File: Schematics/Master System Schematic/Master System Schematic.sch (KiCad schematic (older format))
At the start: 34 parts, among them J1 GND, J2 TS+, J3 TS-, SW1 GLVMS, SW2 SideMounted (BRB), SW3 SideMounted (BRB), U1 CAN_Module

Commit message: Fixed a weird duplicate onto master
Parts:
- removed A1: Arduino_UNO_rev3, symbol NER:Arduino_UNO_rev3
- removed R? (x2): R, symbol Device:R
- removed U1: CAN_Module, symbol NER:CAN-Module
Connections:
- net labels removed: CAN_H, CAN_L, GLV+, GLV_GND, POT1+, POT1-, POT1_INPUT, POT2+, POT2-, POT2_INPUT, Switch1-, Switch2-, Switch_Input1, Switch_Input2
- wire segments 225 -> 165
- no-connect marks 26 -> 0
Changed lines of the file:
@@
 EESchema Schematic File Version 4
+LIBS:Master System Schematic-cache
 EELAYER 30 0
 EELAYER END
@@
 Connection ~ 6150 2350
 Wire Wire Line
-	6150 4800 6150 5100
-Wire Wire Line
 	6150 4400 6150 3550
 Wire Notes Line
@@
 	1    0    0    -1
 $EndComp
-Text HLabel 6600 3050 2    50   Input ~ 0
-GLV+
-Wire Wire Line
-	6600 3050 5550 3050
-Text HLabel 3600 3050 0    50   Input ~ 0
-GLV_GND
-Wire Wire Line
-	3600 3050 4350 3050
-$Comp
-L NER:Arduino_UNO_rev3 A1
-U 1 1 5F6833F8
-P 4950 2900
-F 0 "A1" H 4950 3015 50  0000 C CNN
-F 1 "Arduino_UNO_rev3" H 4950 2924 50  0000 C CNN
-F 2 "" H 4950 3050 50  0001 C CNN
-F 3 "" H 4950 3050 50  0001 C CNN
-	1    4950 2900
-	1    0    0    -1
-$EndComp
-$Comp
-L NER:CAN-Module U1
-U 1 1 5F6A22C3
-P 7600 3100
-F 0 "U1" H 7625 3115 50  0000 C CNN
-F 1 "CAN_Module" H 7625 3024 50  0000 C CNN
-F 2 "" H 7600 3100 50  0001 C CNN
-F 3 "" H 7600 3100 50  0001 C CNN
-	1    7600 3100
-	1    0    0    -1
-$EndComp
-Wire Wire Line
-	7050 3450 5900 3450
-Wire Wire Line
-	5900 3450 5900 3650
-Wire Wire Line
-	5900 3650 5550 3650
-Wire Wire Line
-	7050 3550 6100 3550
-Wire Wire Line
-	6100 3550 6100 3850
-Wire Wire Line
-	6100 3850 5550 3850
-Wire Wire Line
-	7050 3650 6250 3650
-Wire Wire Line
-	6250 3650 6250 3750
-Wire Wire Line
-	6250 3750 5550 3750
-Wire Wire Line
-	7050 3750 6350 3750
-Wire Wire Line
-	6350 3750 6350 3950
-Wire Wire Line
-	7050 3850 6600 3850
-Wire Wire Line
-	6600 3850 6600 3400
-Wire Wire Line
-	6600 3400 5750 3400
-Wire Wire Line
-	5750 3400 5750 3550
-Wire Wire Line
-	5750 3550 5550 3550
-Text HLabel 8950 3650 2    50   Input ~ 0
-CAN_L
-Text HLabel 8950 3500 2    50   Input ~ 0
-CAN_H
-Wire Wire Line
-	8200 3500 8600 3500
-Wire Wire Line
-	8950 3650 8200 3650
-NoConn ~ 4350 3200
-NoConn ~ 4350 3300
-NoConn ~ 4350 3400
-NoConn ~ 4350 3500
-Wire Wire Line
-	5550 4700 5900 4700
-Wire Wire Line
-	5900 4700 5900 4900
-Connection ~ 5900 4700
-$Comp
-L Device:R R?
-U 1 1 5F71A5F5
-P 5900 5050
-F 0 "R?" H 5970 5096 50  0000 L CNN
-F 1 "R" H 5970 5005 50  0000 L CNN
-F 2 "" V 5830 5050 50  0001 C CNN
-F 3 "~" H 5900 5050 50  0001 C CNN
-	1    5900 5050
-	1    0    0    -1
-$EndComp
-$Comp
-L Device:R R?
-U 1 1 5F71A986
-P 6150 5050
-F 0 "R?" H 6220 5096 50  0000 L CNN
-F 1 "R" H 6220 5005 50  0000 L CNN
-F 2 "" V 6080 5050 50  0001 C CNN
-F 3 "~" H 6150 5050 50  0001 C CNN
-	1    6150 5050
-	1    0    0    -1
-$EndComp
-Wire Wire Line
-	5900 5200 5900 5400
-Wire Wire Line
-	5900 5400 6000 5400
-NoConn ~ 7050 3350
-NoConn ~ 5550 3250
-NoConn ~ 5550 3350
-NoConn ~ 5550 3450
-NoConn ~ 4350 3650
-NoConn ~ 4350 3750
-NoConn ~ 4350 3850
-NoConn ~ 4350 3950
-NoConn ~ 4350 4350
-NoConn ~ 4350 4700
-NoConn ~ 4350 4800
-NoConn ~ 4350 4900
-NoConn ~ 4350 5000
-NoConn ~ 5550 5000
-NoConn ~ 5550 4900
-NoConn ~ 5550 4600
-NoConn ~ 5550 4500
-NoConn ~ 5550 4400
-NoConn ~ 5550 4300
-NoConn ~ 5550 4150
-NoConn ~ 5550 4050
-Text HLabel 6800 4700 2    50   Input ~ 0
-Switch_Input1
-Text HLabel 6800 5050 2    50   Input ~ 0
-Switch_Input2
-Wire Wire Line
-	4350 4250 3950 4250
-Wire Wire Line
-	3950 4250 3950 4600
-Wire Wire Line
-	3950 5650 6000 5650
-Wire Wire Line
-	6600 5650 6600 5150
-Wire Wire Line
-	6600 4600 6800 4600
-Wire Wire Line
-	5900 4700 6800 4700
-Wire Wire Line
-	6150 4900 6150 4800
-Wire Wire Line
-	5550 4800 6150 4800
-Wire Wire Line
-	6150 4800 6400 4800
-Wire Wire Line
-	6400 4800 6400 5050
-Wire Wire Line
-	6400 5050 6800 5050
-Connection ~ 6150 4800
-Wire Wire Line
-	6600 5150 6800 5150
-Connection ~ 6600 5150
-Wire Wire Line
-	6600 5150 6600 4600
-Text HLabel 6800 5150 2    50   Input ~ 0
-Switch2-
-Text HLabel 6800 4600 2    50   Input ~ 0
-Switch1-
-Wire Wire Line
-	4350 4500 3300 4500
-Wire Wire Line
-	3950 4600 3300 4600
-Connection ~ 3950 4600
-Wire Wire Line
-	3950 4600 3950 5100
-Wire Wire Line
-	4350 4600 4150 4600
-Wire Wire Line
-	4150 4600 4150 5000
-Wire Wire Line
-	4350 4050 3850 4050
-Wire Wire Line
-	3850 4050 3850 4400
-Wire Wire Line
-	3850 4400 3300 4400
-Wire Wire Line
-	3850 4400 3850 4900
-Wire Wire Line
-	3850 4900 3300 4900
-Connection ~ 3850 4400
-Wire Wire Line
-	3950 5100 3300 5100
-Connection ~ 3950 5100
-Wire Wire Line
-	3950 5100 3950 5650
-Text HLabel 3300 4400 0    50   Input ~ 0
-POT1+
-Text HLabel 3300 4900 0    50   Input ~ 0
-POT2+
-Text HLabel 3300 4500 0    50   Input ~ 0
-POT1_INPUT
-Text HLabel 3300 4600 0    50   Input ~ 0
-POT1-
-Wire Wire Line
-	4150 5000 3300 5000
-Text HLabel 3300 5000 0    50   Input ~ 0
-POT2_INPUT
-Text HLabel 3300 5100 0    50   Input ~ 0
-POT2-
-Wire Wire Line
-	7050 3950 7050 4300
-Wire Wire Line
-	7050 4300 7600 4300
-Wire Wire Line
-	7600 4300 7600 5850
-Wire Wire Line
-	7600 5850 2500 5850
-Wire Wire Line
-	2500 5850 2500 4050
-Wire Wire Line
-	2500 4050 3850 4050
-Connection ~ 3850 4050
-Wire Wire Line
-	6000 5400 6000 5650
-Connection ~ 6000 5400
-Wire Wire Line
-	6000 5400 6150 5400
-Connection ~ 6000 5650
-Wire Wire Line
-	6000 5650 6600 5650
-NoConn ~ 4350 4150
-Wire Wire Line
-	8600 3500 8950 3500
 Wire Wire Line
 	1850 3950 6900 3950
@@
 Wire Wire Line
 	12750 4250 12950 4250
+Wire Wire Line
+	6150 4800 6150 5100
 $EndSCHEMATC

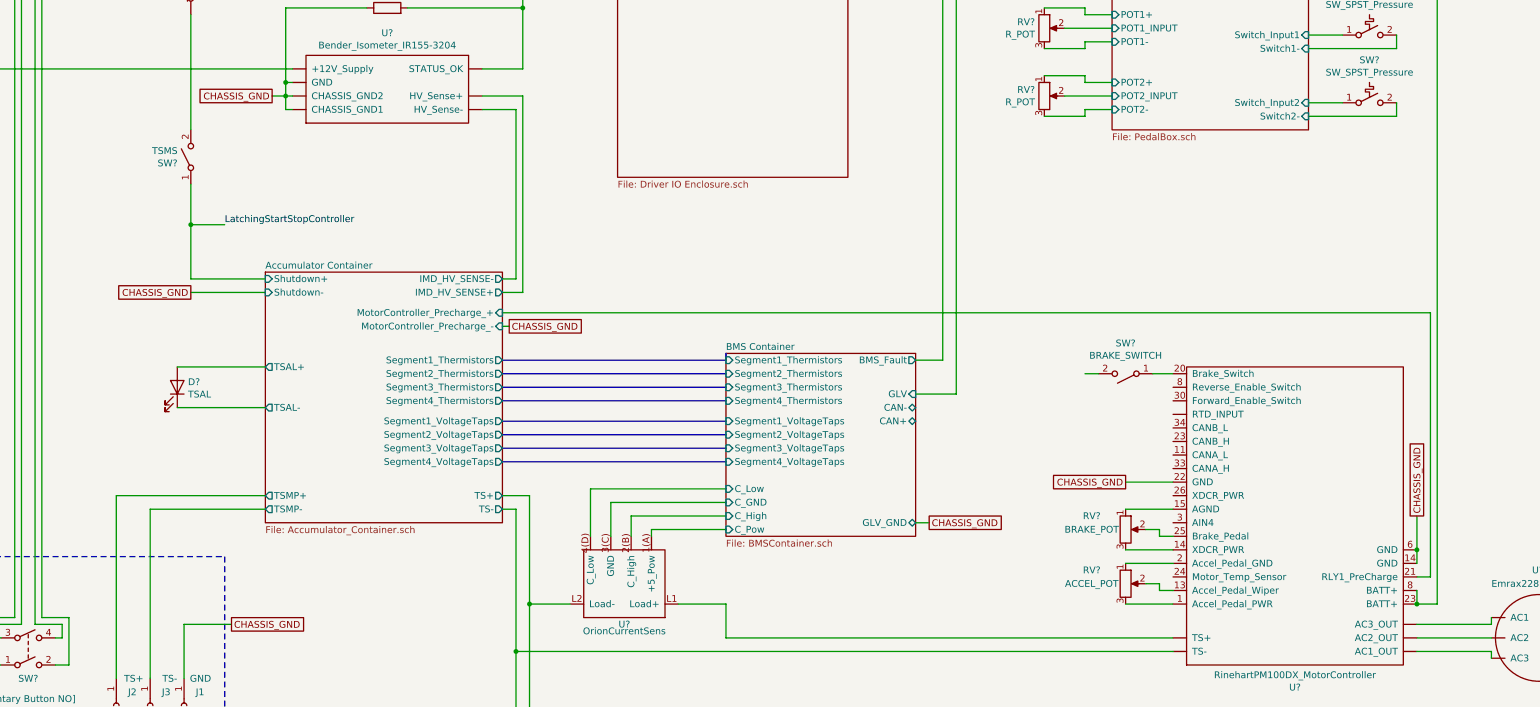
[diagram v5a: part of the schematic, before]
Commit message: integrated matts Battery BOx updates
added MC air control lines
Moved tsal to after imd fuse
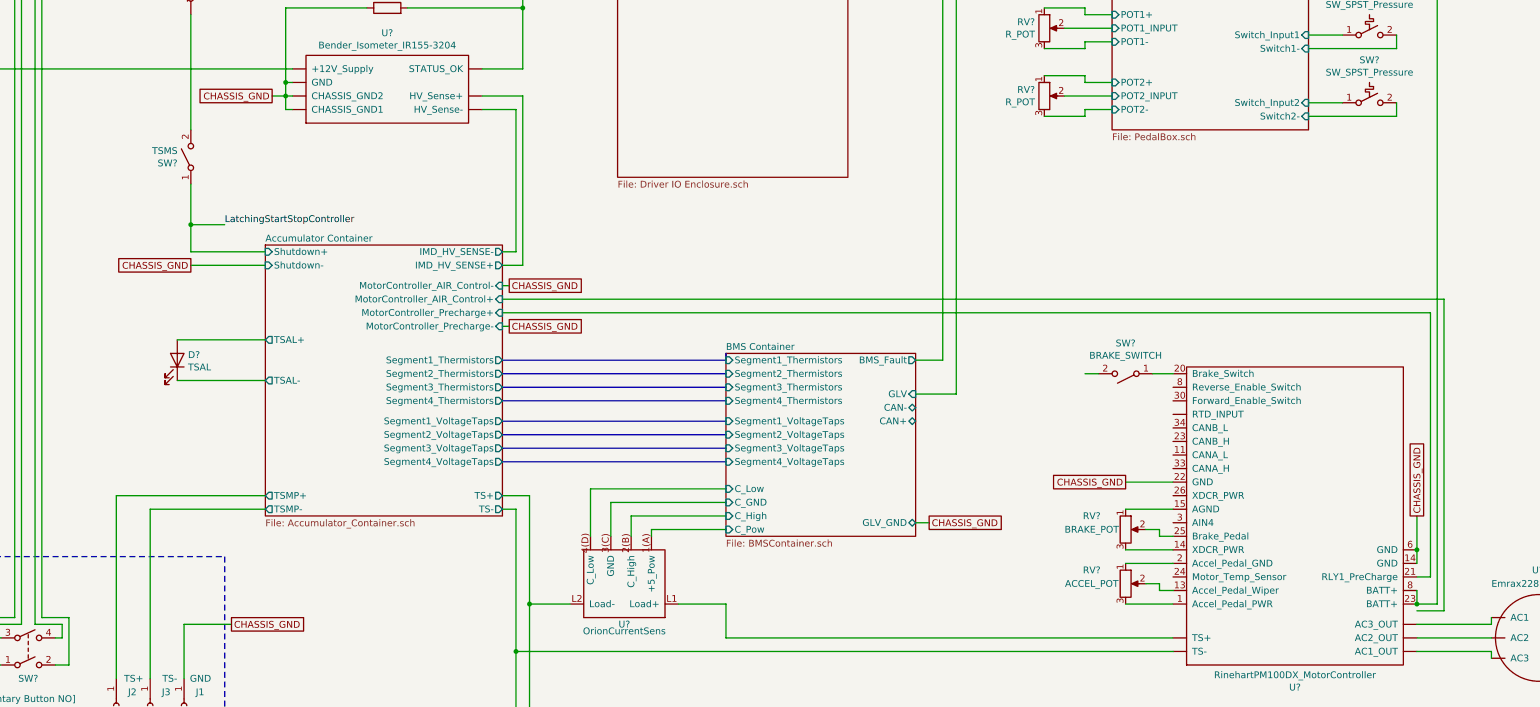
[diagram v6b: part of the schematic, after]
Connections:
- net Accumulator Container/MotorController_Precharge_+ renamed Accumulator Container/MotorController_Precharge+
- new net: U?.23 (CANB_H), U?.6, U?.8 (Reverse_Enable_Switch)
- new net: U?.~ (AC3), U?.~ (TS-) (x2)
- now unconnected: U?.23 (CANB_H), U?.8 (Reverse_Enable_Switch)
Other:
- moved on the sheet: D?
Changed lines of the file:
@@
 EESchema Schematic File Version 4
-LIBS:Master System Schematic-cache
 EELAYER 30 0
 EELAYER END
@@
 Text Notes 4400 8900 0    50   ~ 0
 TSMP and Shutdown Reset Container
-Text GLabel 6150 5600 0    50   UnSpc ~ 0
+Text GLabel 6150 5400 0    50   UnSpc ~ 0
 CHASSIS_GND
 $Comp
@@
 	-1   0    0    1
 $EndComp
-Wire Wire Line
-	6150 5600 6700 5600
 $Sheet
 S 8850 8900 1000 250
@@
 CHASSIS_GND
 $Sheet
-S 6700 5450 1750 1850
+S 6700 5250 1750 2000
 U 5F45B05E
 F0 "Accumulator Container" 50
 F1 "Accumulator_Container.sch" 50
-F2 "MotorController_Precharge_-" I R 8450 5850 50
-F3 "MotorController_Precharge_+" I R 8450 5750 50
-F4 "Shutdown+" I L 6700 5500 50
-F5 "Shutdown-" I L 6700 5600 50
-F6 "TS+" O R 8450 7100 50
-F7 "TS-" O R 8450 7200 50
-F8 "TSAL+" O L 6700 6150 50
-F9 "TSAL-" O L 6700 6450 50
-F10 "IMD_HV_SENSE-" O R 8450 5500 50
-F11 "IMD_HV_SENSE+" O R 8450 5600 50
-F12 "TSMP-" O L 6700 7200 50
-F13 "TSMP+" O L 6700 7100 50
-F14 "Segment1_Thermistors" O R 8450 6100 50
-F15 "Segment2_Thermistors" O R 8450 6200 50
-F16 "Segment3_Thermistors" O R 8450 6300 50
-F17 "Segment4_Thermistors" O R 8450 6400 50
-F18 "Segment1_VoltageTaps" O R 8450 6550 50
-F19 "Segment2_VoltageTaps" O R 8450 6650 50
-F20 "Segment3_VoltageTaps" O R 8450 6750 50
-F21 "Segment4_VoltageTaps" O R 8450 6850 50
+F2 "Shutdown+" I L 6700 5300 50
+F3 "Shutdown-" I L 6700 5400 50
+F4 "TS+" O R 8450 7100 50
+F5 "TS-" O R 8450 7200 50
+F6 "TSAL+" O L 6700 5950 50
+F7 "TSAL-" O L 6700 6250 50
+F8 "IMD_HV_SENSE-" O R 8450 5300 50
+F9 "IMD_HV_SENSE+" O R 8450 5400 50
+F10 "TSMP-" O L 6700 7200 50
+F11 "TSMP+" O L 6700 7100 50
+F12 "Segment1_Thermistors" O R 8450 6100 50
+F13 "Segment2_Thermistors" O R 8450 6200 50
+F14 "Segment3_Thermistors" O R 8450 6300 50
+F15 "Segment4_Thermistors" O R 8450 6400 50
+F16 "Segment1_VoltageTaps" O R 8450 6550 50
+F17 "Segment2_VoltageTaps" O R 8450 6650 50
+F18 "Segment3_VoltageTaps" O R 8450 6750 50
+F19 "Segment4_VoltageTaps" O R 8450 6850 50
+F20 "MotorController_AIR_Control-" I R 8450 5550 50
+F21 "MotorController_AIR_Control+" I R 8450 5650 50
+F22 "MotorController_Precharge-" I R 8450 5850 50
+F23 "MotorController_Precharge+" I R 8450 5750 50
 $EndSheet
 Wire Wire Line
-	8450 5500 8550 5500
-Wire Wire Line
-	8550 5500 8550 4250
-Wire Wire Line
-	8450 5600 8600 5600
-Wire Wire Line
-	8600 5600 8600 4150
+	8450 5300 8550 5300
+Wire Wire Line
+	8450 5400 8600 5400
 Wire Wire Line
 	6150 2350 6250 2350
@@
 	1850 1000 1850 3350
 Wire Wire Line
-	6150 5500 6700 5500
+	6150 5300 6700 5300
 Wire Wire Line
 	8450 7100 8650 7100
@@
 L Device:LED D?
 U 1 1 5FA58D8C
-P 6050 6300
-F 0 "D?" V 6089 6379 50  0000 L CNN
-F 1 "TSAL" V 5998 6379 50  0000 L CNN
-F 2 "" H 6050 6300 50  0001 C CNN
-F 3 "~" H 6050 6300 50  0001 C CNN
-	1    6050 6300
+P 6050 6100
+F 0 "D?" V 6089 6179 50  0000 L CNN
+F 1 "TSAL" V 5998 6179 50  0000 L CNN
+F 2 "" H 6050 6100 50  0001 C CNN
+F 3 "~" H 6050 6100 50  0001 C CNN
+	1    6050 6100
 	0    1    -1   0
 $EndComp
 Wire Wire Line
-	6700 6150 6050 6150
-Wire Wire Line
-	6700 6450 6050 6450
+	6700 5950 6050 5950
+Wire Wire Line
+	6700 6250 6050 6250
 Wire Wire Line
 	15300 5750 15300 7700
@@
 	1850 3950 6900 3950
 Wire Wire Line
-	6150 5100 6150 5500
+	6150 5100 6150 5300
 $Comp
 L Switch:SW_SPST_Temperature SW?
@@
 Wire Wire Line
 	6150 4800 6150 5100
+Wire Wire Line
+	8600 5400 8600 4150
+Wire Wire Line
+	8550 4250 8550 5300
+Text GLabel 8500 5550 2    50   UnSpc ~ 0
+CHASSIS_GND
+Wire Wire Line
+	8500 5550 8450 5550
+Wire Wire Line
+	8450 5650 15400 5650
+Wire Wire Line
+	15400 5650 15400 7950
+Wire Wire Line
+	15400 7950 15200 7950
+Wire Wire Line
+	6150 5400 6700 5400
 $EndSCHEMATC
